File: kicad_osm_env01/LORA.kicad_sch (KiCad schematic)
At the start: 15 parts

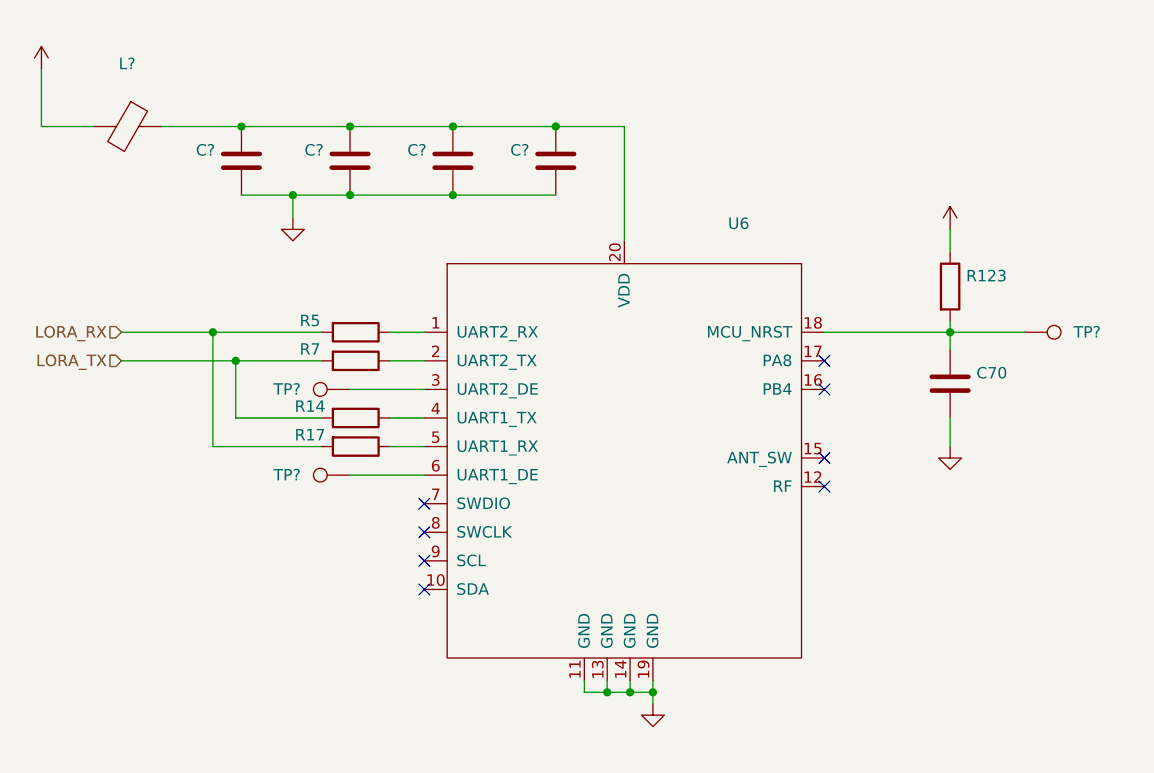
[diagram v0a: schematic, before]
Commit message: added stml433 to schematic and carried out some mods
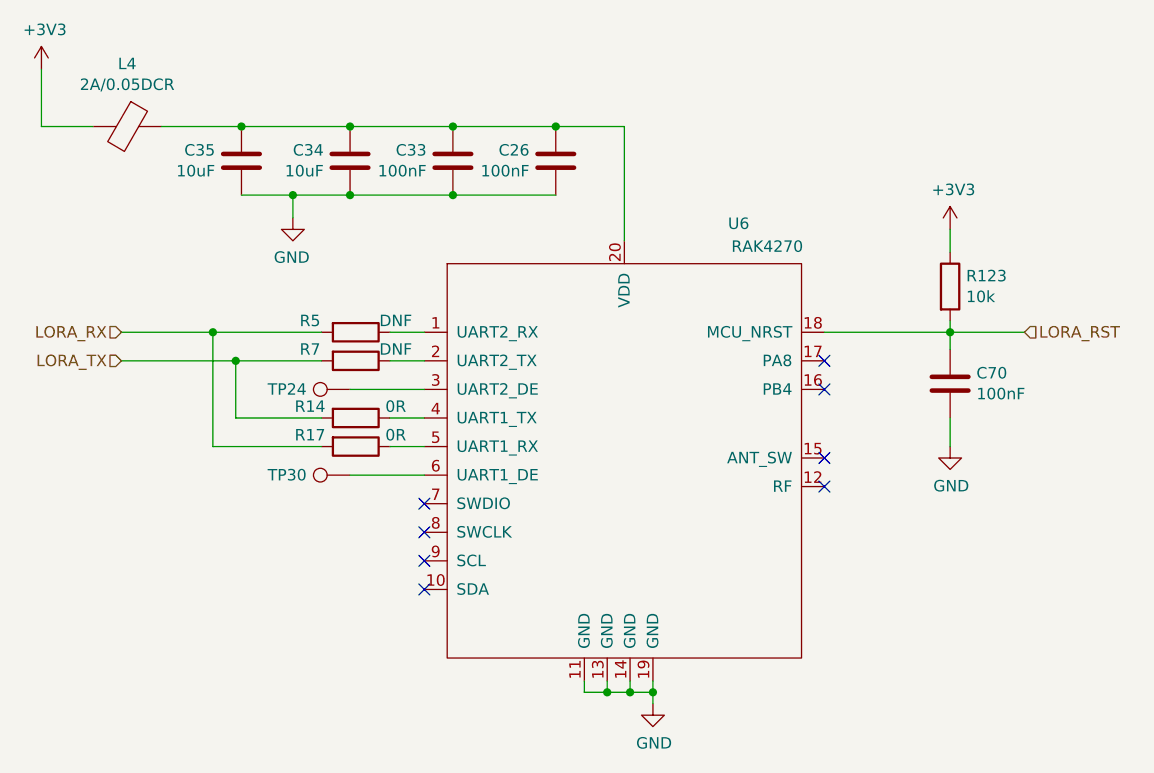
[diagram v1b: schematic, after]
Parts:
- removed TP?: (no value), symbol OSM_env01-rescue:Test_Point-Connector-ESP32-EVB_Rev_D-rescue
- C26, C33: renamed from C?; value (none) -> 100nF; footprint (none) -> Capacitor_SMD:C_0402_1005Metric
- C34, C35: renamed from C?; value (none) -> 10uF; footprint (none) -> Capacitor_SMD:C_0603_1608Metric
- C70: value (none) -> 100nF; footprint (none) -> Capacitor_SMD:C_0402_1005Metric
- L4: renamed from L?; value (none) -> 2A/0.05DCR; footprint (none) -> Inductor_SMD:L_0402_1005Metric
- R123: value (none) -> 10k; footprint (none) -> Resistor_SMD:R_0603_1608Metric
- R14, R17: value (none) -> 0R; footprint (none) -> Resistor_SMD:R_0603_1608Metric
- R5, R7: value (none) -> DNF; footprint (none) -> Resistor_SMD:R_0603_1608Metric
- TP24, TP30: renamed from TP?; value (none) -> Test_Point; footprint (none) -> TestPoint:TestPoint_THTPad_D1.0mm_Drill0.5mm
- U6: value (none) -> RAK4270; footprint (none) -> Devtank_PCB_lib:RAK4270_WisDuo_LPWAN_Module
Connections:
- net LORA_RST: now reaches C70.1, R123.2, U6.18 (MCU_NRST)

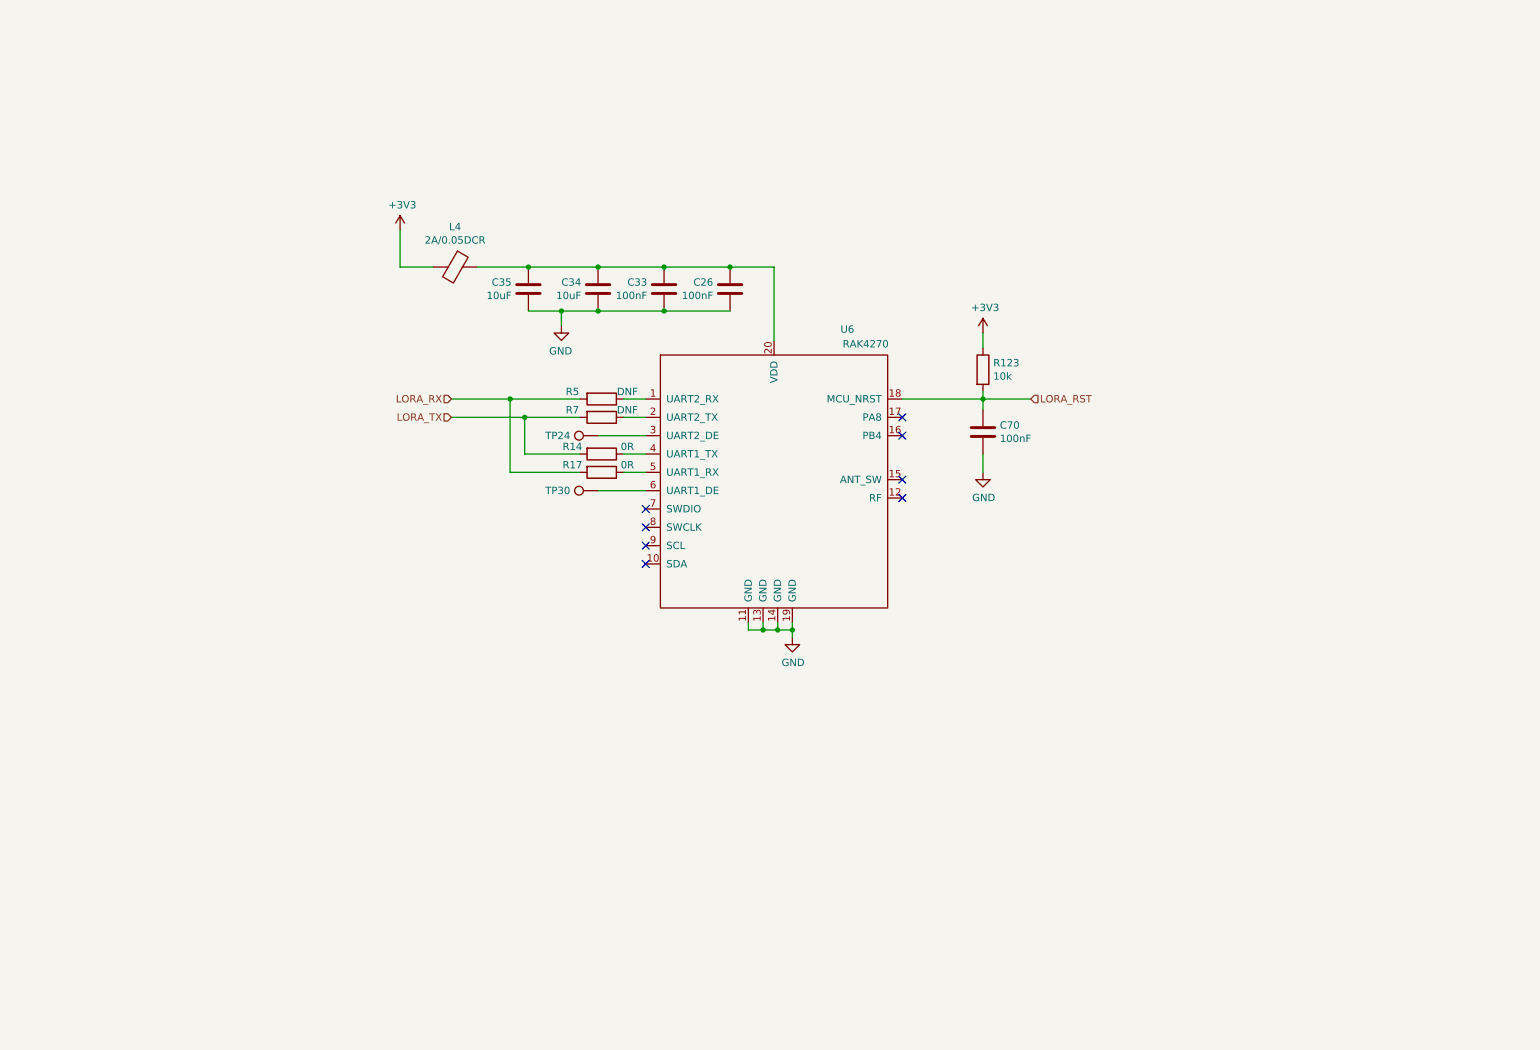
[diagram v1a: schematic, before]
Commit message: updated schematics
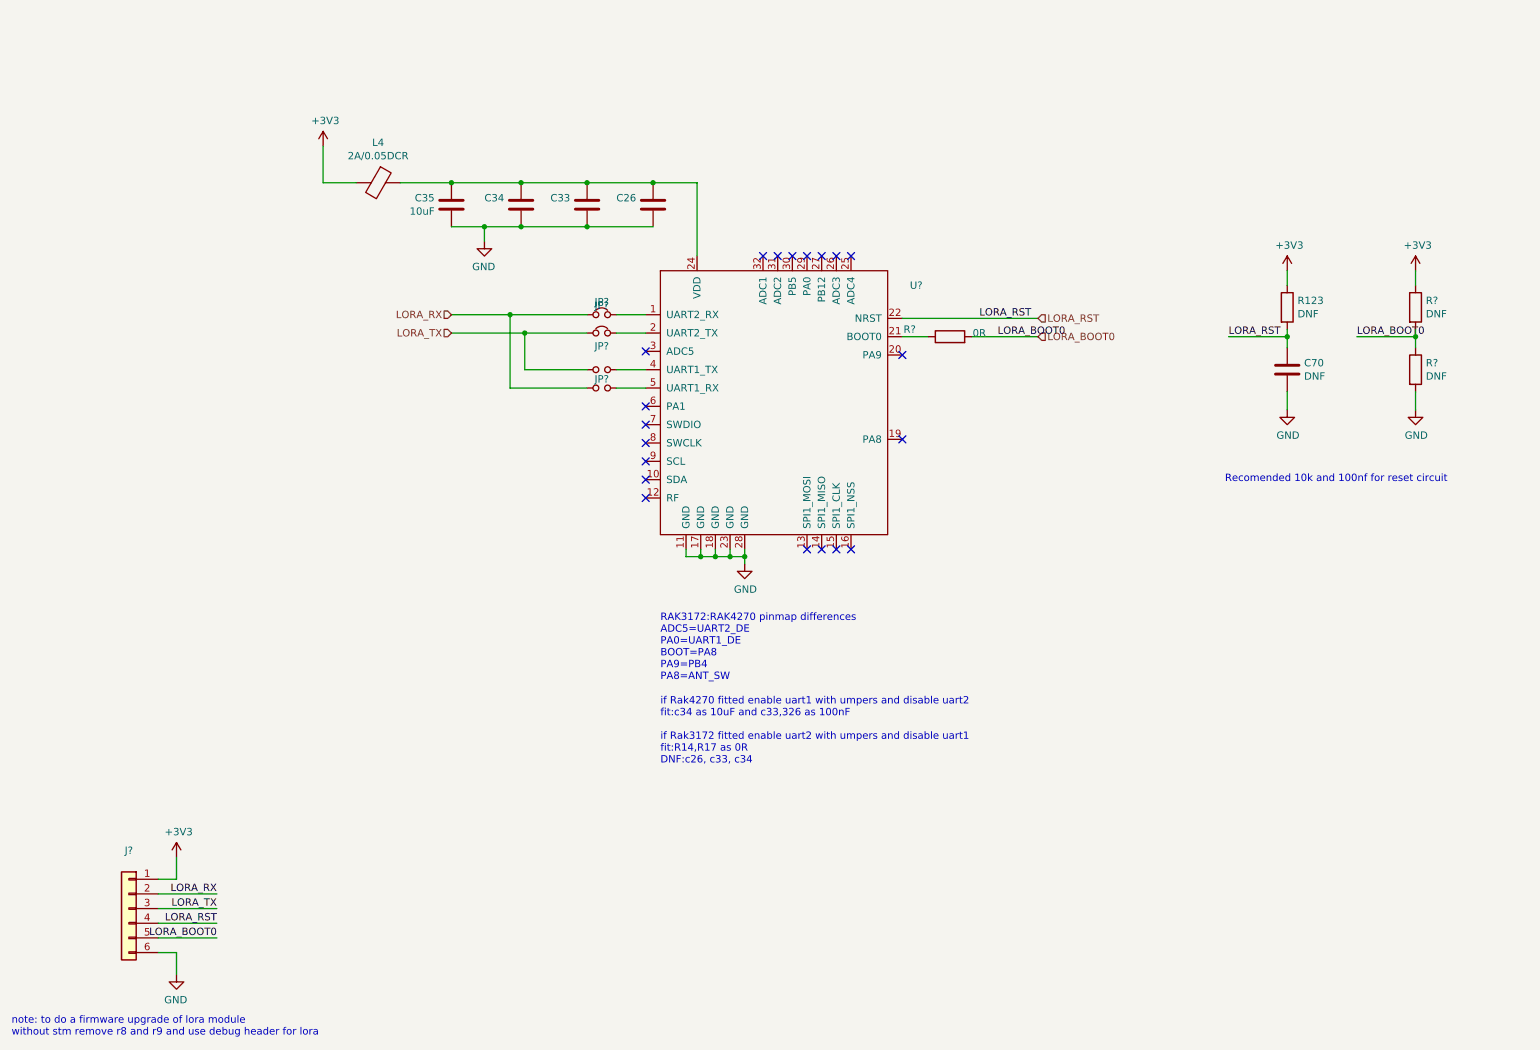
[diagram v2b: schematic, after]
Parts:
- removed R14, R17: 0R, Resistor_SMD:R_0603_1608Metric, symbol device:R
- removed R5, R7: DNF, Resistor_SMD:R_0603_1608Metric, symbol device:R
- removed TP24, TP30: Test_Point, TestPoint:TestPoint_THTPad_D1.0mm_Drill0.5mm, symbol OSM_env01-rescue:Test_Point-Connector-ESP32-EVB_Rev_D-rescue
- removed U6: RAK4270, Devtank_PCB_lib:RAK4270_WisDuo_LPWAN_Module, symbol OSM_env01-rescue:RAK4270-Devtank
- added J?: (no value), symbol Connector:Conn_01x06
- added JP?: ~, symbol device:Jumper_NO_Small
- added JP?: (no value), symbol device:Jumper_NO_Small
- added JP?: (no value), symbol device:Jumper_NC_Small
- added JP?: ~, symbol device:Jumper_NC_Small
- added R? (x2): DNF, Resistor_SMD:R_0603_1608Metric, symbol device:R
- added R?: 0R, symbol device:R
- added U?: (no value), symbol Devtank:RAK3172
- C26, C33: value 100nF -> (none)
- C34: value 10uF -> (none)
- C70: value 100nF -> DNF
- R123: value 10k -> DNF
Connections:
- net +3V3: now also J?.1 (Pin_1), R?.1
- net GND: now also J?.6 (Pin_6), R?.2, U?.11 (GND), U?.17 (GND), U?.18 (GND), U?.23 (GND), U?.28 (GND)
- net LORA_RST: now also J?.4 (Pin_4), U?.22 (NRST)
- net LORA_RX: now also J?.2 (Pin_2), JP?.1, JP?.1
- net LORA_TX: now also J?.3 (Pin_3), JP?.1, JP?.1
- net at C26.1, C33.1, C34.1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: now also U?.24 (VDD)
- new net: JP?.2, U?.4 (UART1_TX)
- new net: JP?.2, U?.5 (UART1_RX)
- new net: JP?.2, U?.1 (UART2_RX)
- new net: JP?.2, U?.2 (UART2_TX)
- new net: R?.1, U?.21 (BOOT0)
- new net LORA_BOOT0: J?.5 (Pin_5), R?.1, R?.2, R?.2
- no-connect marks 8 -> 20
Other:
- note added: "RAK3172:RAK4270 pinmap differences ADC5=UART2_DE PA0=UART1_DE BOOT=PA8 PA9=PB4 PA8=ANT_SW"
- note added: "Recomended 10k and 100nf for reset circuit"
- note added: "if Rak4270 fitted enable uart1 with umpers and disable uart2 fit:c34 as 10uF and c33,326 as 100nF if Rak3172 fitted enable uart2 with umpers and disable uart1 fit:R14,R17 as 0R DNF:c26, c33, c34"
- note added: "note: to do a firmware upgrade of lora module without stm remove r8 and r9 and use debug header for lora"
- moved on the sheet: C26, C33, C34, C35, C70, L4, R123

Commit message: added new battery charge ic u2
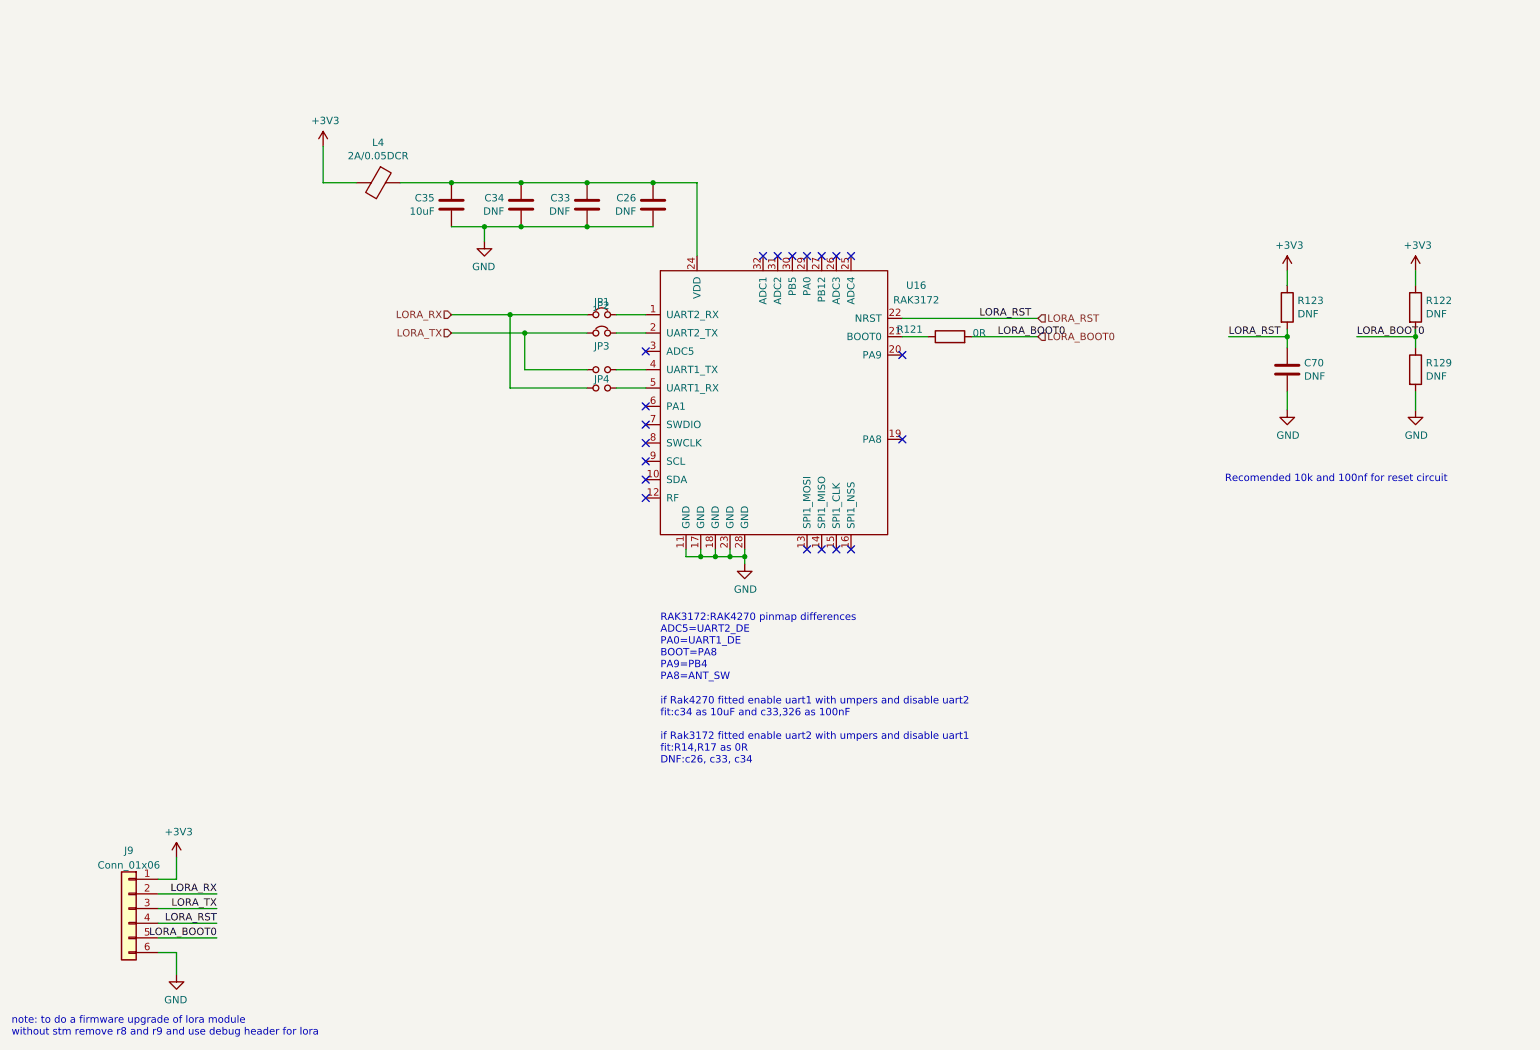
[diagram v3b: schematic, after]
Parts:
- C26, C33, C34: value (none) -> DNF
- J9: renamed from J?; value (none) -> Conn_01x06
- JP1: renamed from JP?; value (none) -> Jumper_NC_Small
- JP4: renamed from JP?; value (none) -> Jumper_NO_Small
- U16: renamed from U?; value (none) -> RAK3172
- gave numbers to parts that had none: 5
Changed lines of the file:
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@@
   (title_block
     (title "Open Smart Monitor")
-    (date "2021-09-29")
-    (rev "B")
+    (date "2022-07-01")
+    (rev "C")
     (company "Devtank LTD")
     (comment 1 "Part No: 304-010")
@@
       (effects (font (size 1.27 1.27)) (justify left))
     )
-    (property "Value" "" (id 1) (at 123.444 50.673 0)
+    (property "Value" "DNF" (id 1) (at 123.444 50.673 0)
       (effects (font (size 1.27 1.27)) (justify left))
     )
@@
       (effects (font (size 1.27 1.27)) (justify left))
     )
-    (property "Value" "" (id 1) (at 112.014 50.673 0)
+    (property "Value" "DNF" (id 1) (at 112.014 50.673 0)
       (effects (font (size 1.27 1.27)) (justify left))
     )
@@
       (effects (font (size 1.27 1.27)) (justify left))
     )
-    (property "Value" "" (id 1) (at 100.584 50.673 0)
+    (property "Value" "DNF" (id 1) (at 100.584 50.673 0)
       (effects (font (size 1.27 1.27)) (justify left))
     )
@@
   (symbol (lib_id "device:Jumper_NO_Small") (at 117.475 78.105 0) (unit 1)
     (in_bom yes) (on_board yes) (fields_autoplaced)
-    (property "Reference" "JP?" (id 0) (at 117.475 74.0242 0))
+    (property "Reference" "JP3" (id 0) (at 117.475 74.0242 0))
     (property "Value" "~" (id 1) (at 117.475 76.5611 0))
     (property "Footprint" "" (id 2) (at 117.475 78.105 0)
@@
   (symbol (lib_id "device:Jumper_NO_Small") (at 117.475 81.28 0) (unit 1)
     (in_bom yes) (on_board yes) (fields_autoplaced)
-    (property "Reference" "JP?" (id 0) (at 117.475 79.7362 0))
-    (property "Value" "" (id 1) (at 117.475 79.7361 0)
+    (property "Reference" "JP4" (id 0) (at 117.475 79.7362 0))
+    (property "Value" "Jumper_NO_Small" (id 1) (at 117.475 79.7361 0)
       (effects (font (size 1.27 1.27)) hide)
     )
@@
   (symbol (lib_id "device:R") (at 258.445 78.105 0) (unit 1)
     (in_bom yes) (on_board yes)
-    (property "Reference" "R?" (id 0) (at 260.223 76.9366 0)
+    (property "Reference" "R129" (id 0) (at 260.223 76.9366 0)
       (effects (font (size 1.27 1.27)) (justify left))
     )
@@
   (symbol (lib_id "Devtank:RAK3172") (at 147.32 83.185 0) (unit 1)
     (in_bom yes) (on_board yes) (fields_autoplaced)
-    (property "Reference" "U?" (id 0) (at 171.9527 63.5085 0))
-    (property "Value" "" (id 1) (at 171.9527 66.0454 0))
+    (property "Reference" "U16" (id 0) (at 171.9527 63.5085 0))
+    (property "Value" "RAK3172" (id 1) (at 171.9527 66.0454 0))
     (property "Footprint" "" (id 2) (at 140.97 71.755 0)
       (effects (font (size 1.27 1.27)) hide)
@@
   (symbol (lib_id "device:R") (at 258.445 67.31 0) (unit 1)
     (in_bom yes) (on_board yes)
-    (property "Reference" "R?" (id 0) (at 260.223 66.1416 0)
+    (property "Reference" "R122" (id 0) (at 260.223 66.1416 0)
       (effects (font (size 1.27 1.27)) (justify left))
     )
@@
   (symbol (lib_id "device:Jumper_NC_Small") (at 117.475 68.58 0) (unit 1)
     (in_bom yes) (on_board yes) (fields_autoplaced)
-    (property "Reference" "JP?" (id 0) (at 117.475 66.3614 0))
-    (property "Value" "" (id 1) (at 117.475 66.3613 0)
+    (property "Reference" "JP1" (id 0) (at 117.475 66.3614 0))
+    (property "Value" "Jumper_NC_Small" (id 1) (at 117.475 66.3613 0)
       (effects (font (size 1.27 1.27)) hide)
     )
@@
   (symbol (lib_id "device:Jumper_NC_Small") (at 117.475 71.755 0) (unit 1)
     (in_bom yes) (on_board yes) (fields_autoplaced)
-    (property "Reference" "JP?" (id 0) (at 117.475 66.9994 0))
+    (property "Reference" "JP2" (id 0) (at 117.475 66.9994 0))
     (property "Value" "~" (id 1) (at 117.475 69.5363 0))
     (property "Footprint" "" (id 2) (at 117.475 71.755 0)
@@
   (symbol (lib_id "OSM_env01:GND") (at 43.815 182.88 0) (mirror y) (unit 1)
     (in_bom yes) (on_board yes)
-    (property "Reference" "#PWR?" (id 0) (at 43.815 189.23 0)
+    (property "Reference" "#PWR098" (id 0) (at 43.815 189.23 0)
       (effects (font (size 1.27 1.27)) hide)
     )
@@
   (symbol (lib_id "Connector:Conn_01x06") (at 35.56 171.45 0) (mirror y) (unit 1)
     (in_bom yes) (on_board yes) (fields_autoplaced)
-    (property "Reference" "J?" (id 0) (at 35.56 161.4002 0))
-    (property "Value" "" (id 1) (at 35.56 163.9371 0))
+    (property "Reference" "J9" (id 0) (at 35.56 161.4002 0))
+    (property "Value" "Conn_01x06" (id 1) (at 35.56 163.9371 0))
     (property "Footprint" "" (id 2) (at 35.56 171.45 0)
       (effects (font (size 1.27 1.27)) hide)
@@
   (symbol (lib_id "device:R") (at 177.8 72.39 90) (unit 1)
     (in_bom yes) (on_board yes)
-    (property "Reference" "R?" (id 0) (at 170.815 71.12 90))
+    (property "Reference" "R121" (id 0) (at 170.815 71.12 90))
     (property "Value" "0R" (id 1) (at 182.88 71.755 90))
     (property "Footprint" "" (id 2) (at 177.8 74.168 90)
@@
   (symbol (lib_id "power:GND") (at 258.445 85.09 0) (unit 1)
     (in_bom yes) (on_board yes)
-    (property "Reference" "#PWR?" (id 0) (at 258.445 91.44 0)
+    (property "Reference" "#PWR0100" (id 0) (at 258.445 91.44 0)
       (effects (font (size 1.27 1.27)) hide)
     )
@@
   (symbol (lib_id "power:+3V3") (at 258.445 60.96 0) (unit 1)
     (in_bom yes) (on_board yes)
-    (property "Reference" "#PWR?" (id 0) (at 258.445 64.77 0)
+    (property "Reference" "#PWR099" (id 0) (at 258.445 64.77 0)
       (effects (font (size 1.27 1.27)) hide)
     )
@@
   (symbol (lib_id "power:+3V3") (at 43.815 162.56 0) (unit 1)
     (in_bom yes) (on_board yes)
-    (property "Reference" "#PWR?" (id 0) (at 43.815 166.37 0)
-      (effects (font (size 1.27 1.27)) hide)
-    )
+    (property "Reference" "#PWR097" (id 0) (at 43.815 166.37 0)
+      (effects (font (size 1.27 1.27)) hide)
+    )
